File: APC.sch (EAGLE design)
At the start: 12 parts, among them IC1 NE556D, J1 POWER_JACKPTH_SMD_COMBO, J3 AUDIO_JACK_3.5MM_PTH, P1 1M, P2 1M, P3 100k

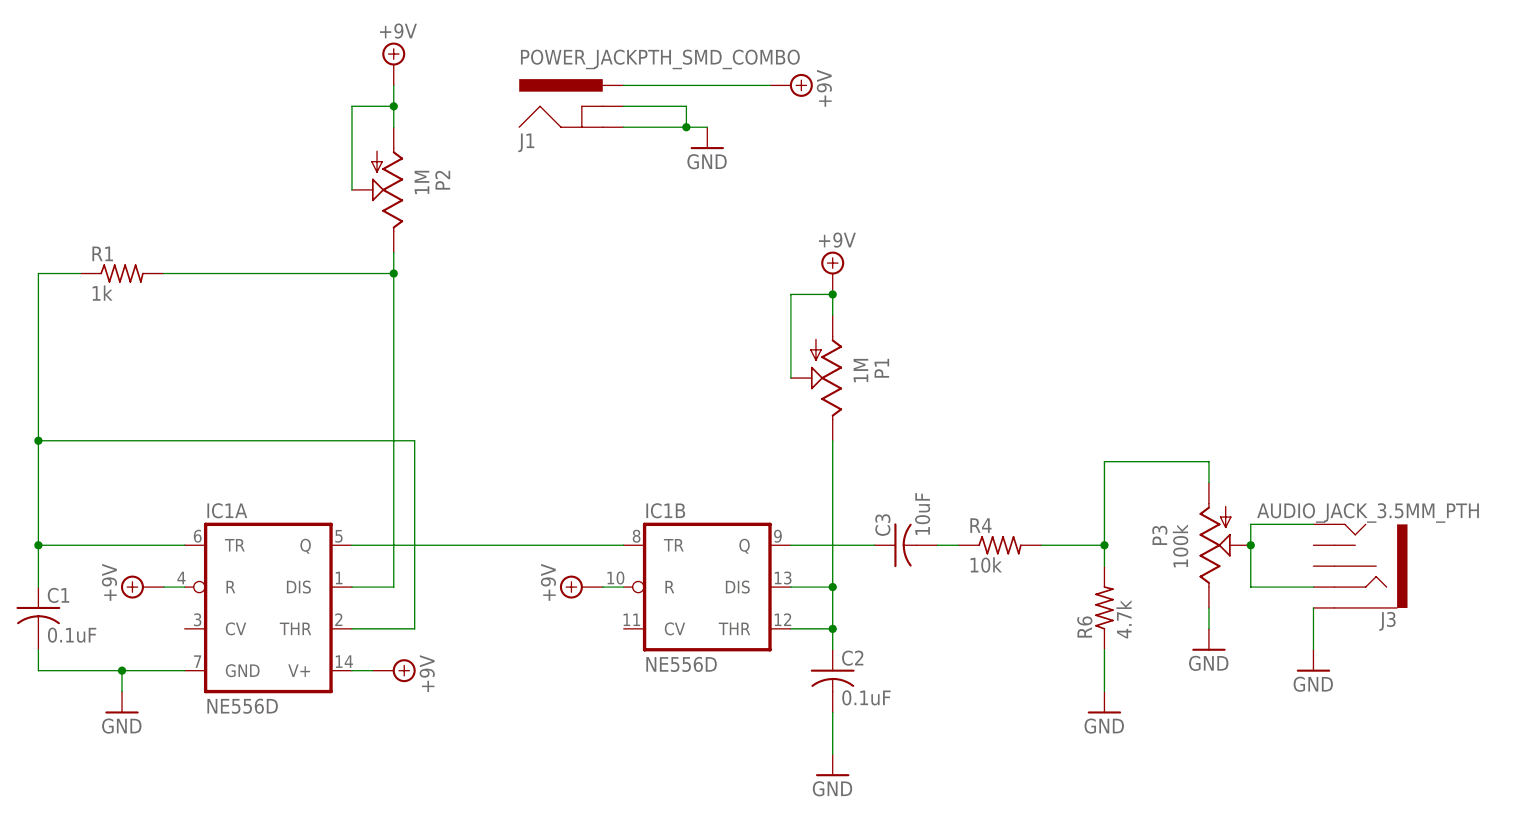
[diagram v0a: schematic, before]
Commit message: V2
Updated schematic to use all digikey parts. Added solderable pads for power
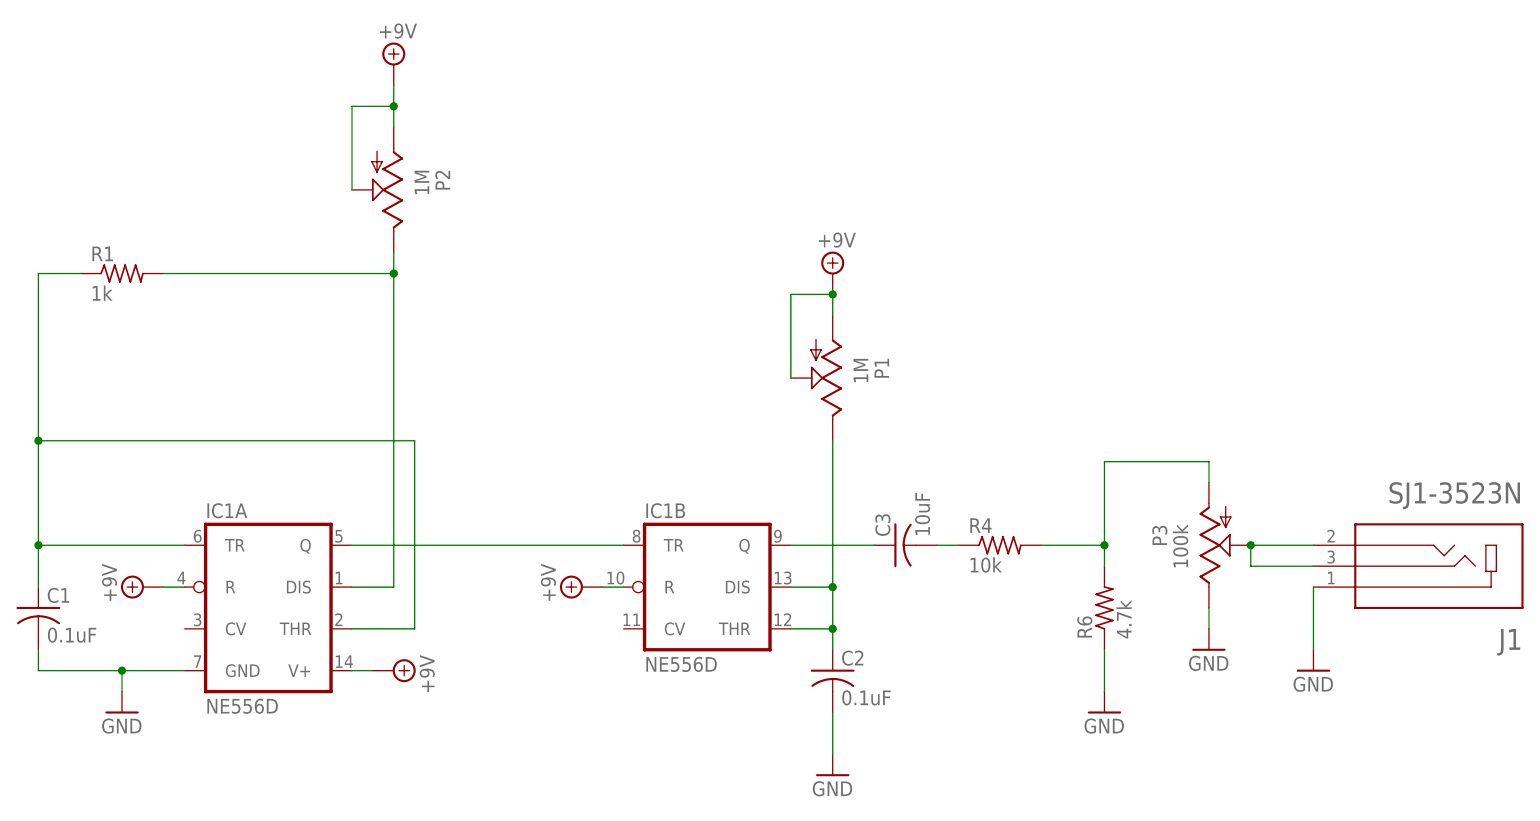
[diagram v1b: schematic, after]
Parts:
- removed J3: AUDIO_JACK_3.5MM_PTH, SparkFun-Connectors:AUDIO_JACK_3.5MM_PTH
- J1: value POWER_JACKPTH_SMD_COMBO -> SJ1-3523N; device SparkFun-Connectors:POWER_JACKPTH_SMD_COMBO -> SJ1-3523N:SJ1-3523N
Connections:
- net +9V: no longer J1.PWR
- net GND: now also J1.1; no longer J1.GND, J1.GNDBREAK, J3.SLEEVE
- net N$9: now also J1.2, J1.3; no longer J3.RING, J3.TIP
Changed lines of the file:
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@@
 <part name="GND6" library="supply1" library_urn="urn:adsk.eagle:library:371" deviceset="GND" device=""/>
 <part name="R6" library="rcl" library_urn="urn:adsk.eagle:library:334" deviceset="R-US_" device="R0805" package3d_urn="urn:adsk.eagle:package:23553/2" value="4.7k"/>
-<part name="J3" library="SparkFun-Connectors" library_urn="urn:adsk.eagle:library:513" deviceset="AUDIO_JACK_3.5MM" device="_PTH" package3d_urn="urn:adsk.eagle:package:37997/1"/>
-<part name="J1" library="SparkFun-Connectors" library_urn="urn:adsk.eagle:library:513" deviceset="POWER_JACK" device="PTH_SMD_COMBO" package3d_urn="urn:adsk.eagle:package:38223/1"/>
-<part name="SUPPLY1" library="supply2" library_urn="urn:adsk.eagle:library:372" deviceset="+9V" device=""/>
-<part name="GND3" library="supply1" library_urn="urn:adsk.eagle:library:371" deviceset="GND" device=""/>
+<part name="J1" library="SJ1-3523N" deviceset="SJ1-3523N" device=""/>
 </parts>
 <sheets>
@@
 <attribute name="VALUE" x="191.262" y="64.77" size="1.778" layer="96" rot="R90"/>
 </instance>
-<instance part="J3" gate="G$1" x="218.44" y="73.66" smashed="yes" rot="R180">
-<attribute name="NAME" x="223.52" y="68.072" size="1.778" layer="95" font="vector" rot="R180"/>
-<attribute name="VALUE" x="233.68" y="81.28" size="1.778" layer="96" font="vector" rot="R180"/>
-</instance>
-<instance part="J1" gate="G$1" x="127" y="124.46" smashed="yes">
-<attribute name="VALUE" x="116.84" y="134.62" size="1.778" layer="96" font="vector"/>
-<attribute name="NAME" x="116.84" y="124.46" size="1.778" layer="95" font="vector"/>
-</instance>
-<instance part="SUPPLY1" gate="G$1" x="149.86" y="132.08" smashed="yes" rot="R270">
-<attribute name="VALUE" x="153.035" y="133.985" size="1.778" layer="96" rot="R270"/>
-</instance>
-<instance part="GND3" gate="1" x="139.7" y="124.46" smashed="yes">
-<attribute name="VALUE" x="137.16" y="121.92" size="1.778" layer="96"/>
+<instance part="J1" gate="G$1" x="228.6" y="73.66" smashed="yes" rot="R180">
+<attribute name="NAME" x="238.7689" y="66.03335" size="2.54221875" layer="95" rot="R180"/>
+<attribute name="VALUE" x="238.7653" y="83.8253" size="2.541340625" layer="96" rot="R180"/>
 </instance>
 </instances>
@@
 </segment>
 <segment>
-<wire x1="213.36" y1="68.58" x2="213.36" y2="63.5" width="0.1524" layer="91"/>
+<wire x1="213.36" y1="71.12" x2="213.36" y2="63.5" width="0.1524" layer="91"/>
 <pinref part="GND1" gate="1" pin="GND"/>
-<pinref part="J3" gate="G$1" pin="SLEEVE"/>
+<pinref part="J1" gate="G$1" pin="1"/>
 </segment>
 <segment>
@@
 <wire x1="200.66" y1="68.58" x2="200.66" y2="66.04" width="0.1524" layer="91"/>
 <pinref part="GND6" gate="1" pin="GND"/>
-</segment>
-<segment>
-<pinref part="J1" gate="G$1" pin="GNDBREAK"/>
-<wire x1="129.54" y1="129.54" x2="137.16" y2="129.54" width="0.1524" layer="91"/>
-<wire x1="137.16" y1="129.54" x2="137.16" y2="127" width="0.1524" layer="91"/>
-<pinref part="J1" gate="G$1" pin="GND"/>
-<wire x1="137.16" y1="127" x2="129.54" y2="127" width="0.1524" layer="91"/>
-<pinref part="GND3" gate="1" pin="GND"/>
-<wire x1="137.16" y1="127" x2="139.7" y2="127" width="0.1524" layer="91"/>
-<junction x="137.16" y="127"/>
 </segment>
 </net>
@@
 <pinref part="SUPPLY6" gate="G$1" pin="+9V"/>
 <junction x="154.94" y="106.68"/>
-</segment>
-<segment>
-<pinref part="J1" gate="G$1" pin="PWR"/>
-<wire x1="129.54" y1="132.08" x2="147.32" y2="132.08" width="0.1524" layer="91"/>
-<pinref part="SUPPLY1" gate="G$1" pin="+9V"/>
 </segment>
 </net>
@@
 <net name="N$9" class="0">
 <segment>
-<wire x1="213.36" y1="78.74" x2="205.74" y2="78.74" width="0.1524" layer="91"/>
 <pinref part="P3" gate="G$1" pin="S"/>
-<wire x1="205.74" y1="78.74" x2="205.74" y2="76.2" width="0.1524" layer="91"/>
-<wire x1="205.74" y1="76.2" x2="205.74" y2="71.12" width="0.1524" layer="91"/>
-<wire x1="205.74" y1="71.12" x2="213.36" y2="71.12" width="0.1524" layer="91"/>
+<wire x1="205.74" y1="76.2" x2="205.74" y2="73.66" width="0.1524" layer="91"/>
 <junction x="205.74" y="76.2"/>
-<pinref part="J3" gate="G$1" pin="RING"/>
-<pinref part="J3" gate="G$1" pin="TIP"/>
+<pinref part="J1" gate="G$1" pin="3"/>
+<wire x1="213.36" y1="73.66" x2="205.74" y2="73.66" width="0.1524" layer="91"/>
+<pinref part="J1" gate="G$1" pin="2"/>
+<wire x1="213.36" y1="76.2" x2="205.74" y2="76.2" width="0.1524" layer="91"/>
 </segment>
 </net>
@@
 </sheet>
 </sheets>
+<errors>
+</errors>
 </schematic>
 </drawing>

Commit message: JLC Gerber created
Ready for ordering
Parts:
- renumbered R4 to R2, R6 to R3
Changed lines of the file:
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@@
 <part name="SUPPLY6" library="supply2" library_urn="urn:adsk.eagle:library:372" deviceset="+9V" device=""/>
 <part name="C3" library="rcl" library_urn="urn:adsk.eagle:library:334" deviceset="C-US" device="C0805" package3d_urn="urn:adsk.eagle:package:23617/2" value="10uF"/>
-<part name="R4" library="rcl" library_urn="urn:adsk.eagle:library:334" deviceset="R-US_" device="R0805" package3d_urn="urn:adsk.eagle:package:23553/2" value="10k"/>
+<part name="R2" library="rcl" library_urn="urn:adsk.eagle:library:334" deviceset="R-US_" device="R0805" package3d_urn="urn:adsk.eagle:package:23553/2" value="10k"/>
 <part name="GND5" library="supply1" library_urn="urn:adsk.eagle:library:371" deviceset="GND" device=""/>
 <part name="GND1" library="supply1" library_urn="urn:adsk.eagle:library:371" deviceset="GND" device=""/>
 <part name="P3" library="pot" library_urn="urn:adsk.eagle:library:331" deviceset="TRIM_US-" device="PT10" package3d_urn="urn:adsk.eagle:package:22715/1" value="100k"/>
 <part name="GND6" library="supply1" library_urn="urn:adsk.eagle:library:371" deviceset="GND" device=""/>
-<part name="R6" library="rcl" library_urn="urn:adsk.eagle:library:334" deviceset="R-US_" device="R0805" package3d_urn="urn:adsk.eagle:package:23553/2" value="4.7k"/>
+<part name="R3" library="rcl" library_urn="urn:adsk.eagle:library:334" deviceset="R-US_" device="R0805" package3d_urn="urn:adsk.eagle:package:23553/2" value="4.7k"/>
 <part name="J1" library="SJ1-3523N" deviceset="SJ1-3523N" device=""/>
 </parts>
@@
 <attribute name="VALUE" x="166.751" y="77.216" size="1.778" layer="96" rot="R90"/>
 </instance>
-<instance part="R4" gate="G$1" x="175.26" y="76.2" smashed="yes">
+<instance part="R2" gate="G$1" x="175.26" y="76.2" smashed="yes">
 <attribute name="NAME" x="171.45" y="77.6986" size="1.778" layer="95"/>
 <attribute name="VALUE" x="171.45" y="72.898" size="1.778" layer="96"/>
@@
 <attribute name="VALUE" x="198.12" y="60.96" size="1.778" layer="96"/>
 </instance>
-<instance part="R6" gate="G$1" x="187.96" y="68.58" smashed="yes" rot="R90">
+<instance part="R3" gate="G$1" x="187.96" y="68.58" smashed="yes" rot="R90">
 <attribute name="NAME" x="186.4614" y="64.77" size="1.778" layer="95" rot="R90"/>
 <attribute name="VALUE" x="191.262" y="64.77" size="1.778" layer="96" rot="R90"/>
@@
 <segment>
 <pinref part="GND5" gate="1" pin="GND"/>
-<pinref part="R6" gate="G$1" pin="1"/>
+<pinref part="R3" gate="G$1" pin="1"/>
 <wire x1="187.96" y1="58.42" x2="187.96" y2="63.5" width="0.1524" layer="91"/>
 </segment>
@@
 <segment>
 <pinref part="C3" gate="G$1" pin="2"/>
-<pinref part="R4" gate="G$1" pin="1"/>
+<pinref part="R2" gate="G$1" pin="1"/>
 <wire x1="167.64" y1="76.2" x2="170.18" y2="76.2" width="0.1524" layer="91"/>
 </segment>
@@
 <net name="N$10" class="0">
 <segment>
-<pinref part="R4" gate="G$1" pin="2"/>
+<pinref part="R2" gate="G$1" pin="2"/>
 <wire x1="180.34" y1="76.2" x2="187.96" y2="76.2" width="0.1524" layer="91"/>
 <wire x1="187.96" y1="76.2" x2="187.96" y2="86.36" width="0.1524" layer="91"/>
@@
 <wire x1="200.66" y1="86.36" x2="200.66" y2="83.82" width="0.1524" layer="91"/>
 <wire x1="187.96" y1="76.2" x2="187.96" y2="73.66" width="0.1524" layer="91"/>
-<pinref part="R6" gate="G$1" pin="2"/>
-</segment>
-</net>
+<pinref part="R3" gate="G$1" pin="2"/>
+</segment>
+</net>
